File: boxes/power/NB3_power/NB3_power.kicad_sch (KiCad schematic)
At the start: 74 parts, among them J1 Barrel_Jack_PJ-036AH-SMT-TR, J2 Conn_01x02_Male, J3 Conn_01x02_Male, J4 Conn_01x02_Male, J5 Conn_01x04_Male, J6 Conn_01x02_Male, J7 Conn_01x02_Male, Q1 Q_PMOS_GDS, Q2 Q_NMOS_GDS, SW1 SW_SPDT, SW2 SW_SPDT, U1 NiMH_Charger_LTC4010, U2 Voltage_Regulator_AP64501

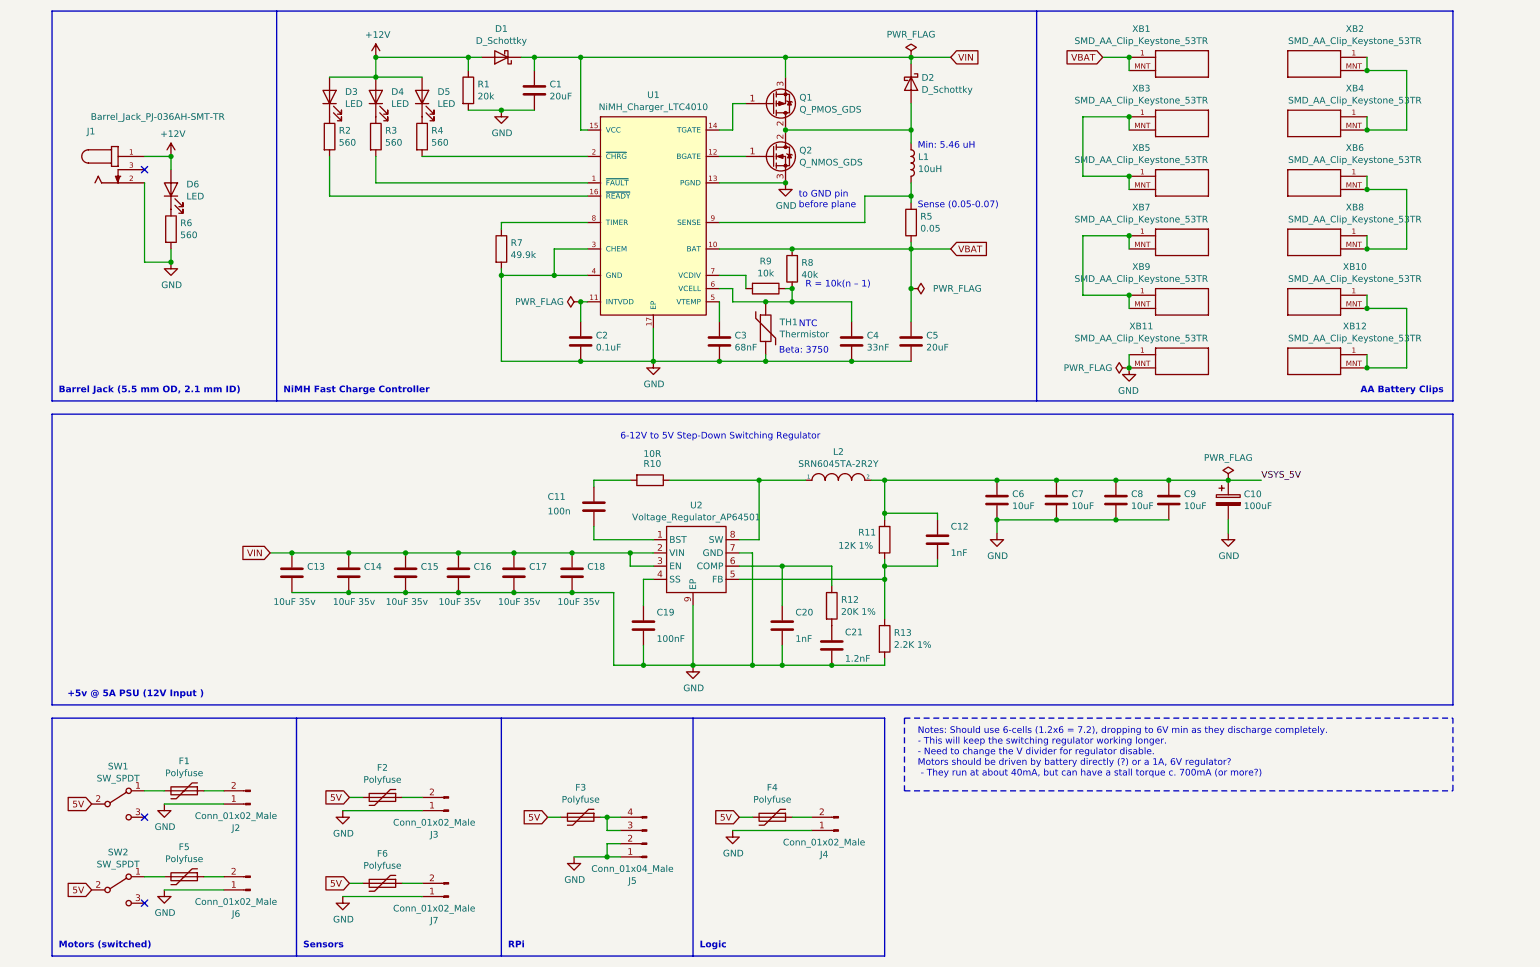
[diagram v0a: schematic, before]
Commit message: Work on NB3_power PCB
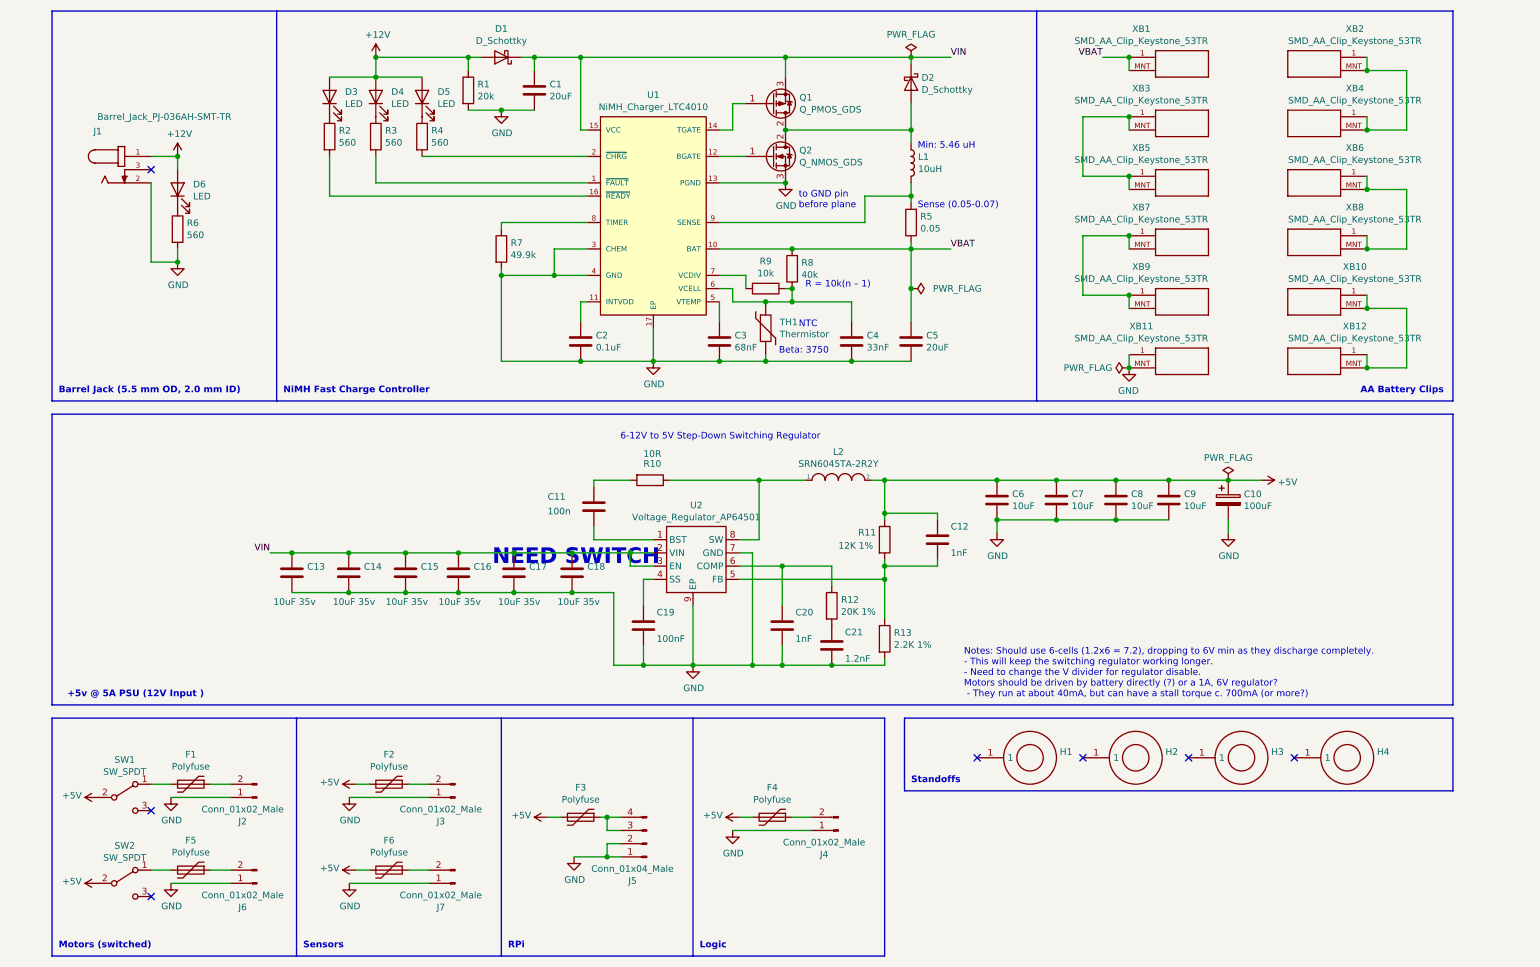
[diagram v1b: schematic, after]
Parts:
- added H1, H2, H3, H4: Standoff_SMT_5H_M2.5_9774050151R, NB3_power:Standoff_SMT_5H_M2.5_9774050151R, symbol NB3_power:Standoff_SMT_5H_M2.5_9774050151R
- Q1: footprint (none) -> NB3_power:PMOS_SMD_FDC658AP
- Q2: footprint (none) -> NB3_power:NMOS_SMD_SI3410DV-T1-GE3
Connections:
- net VSYS_5V is gone; now on net +5V: C10.1, C12.1, C6.1, C7.1, C8.1, C9.1, L2.2, R11.1
- net 5V renamed +5V
- no-connect marks 3 -> 7
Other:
- note added: "Barrel Jack (5.5 mm OD, 2.0 mm ID)"
- note added: "NEED SWITCH"
- note added: "Standoffs"
- note removed: "Barrel Jack (5.5 mm OD, 2.1 mm ID)"
- moved on the sheet: D6, F1, F2, F5, F6, J1, J2, J3, J6, J7, R6, SW1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

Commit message: More work on NB3_power PCB
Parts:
- removed D1, D2: D_Schottky, Diode_SMD:D_0805_2012Metric, symbol Device:D_Schottky
- removed SW2: SW_SPDT, NB3_power:Switch_SPDT_SMD_Slide_JS102011JCQN, symbol Switch:SW_SPDT
- added CR1, CR2: Schottky_PMEG3050EP,115, NB3_power:Schottky_PMEG3050EP,115, symbol NB3_power:Schottky_PMEG3050EP,115
- F1, F2, F4, F5, F6: value Polyfuse -> 1.1h2.2t
- F3: value Polyfuse -> 3h5t; footprint Fuse:Fuse_0805_2012Metric -> Fuse:Fuse_Bourns_MF-SM_7.98x5.44mm
- R8: value 40k -> 50k
- TH1: value Thermistor -> 10k, 3750; footprint (none) -> Resistor_SMD:R_0603_1608Metric
- renumbered C5 to C2, C2 to C3, C3 to C5, D3 to D1, D4 to D2, D5 to D3, D6 to D4, R6 to R5, R5 to R6
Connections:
- net +12V: now also CR1.2
- net +5V: now also F1.2, F5.2; no longer SW1.2 (B)
- net GND: now also SW1.3 (C)
- net VBAT: now also CR2.2
- net VIN: now also L1.1, Q1.2 (D), Q2.2 (D), SW1.1 (A), CR1.1, CR2.1; no longer U2.3 (EN)
- net at C5.1, U1.5 (VTEMP): now also C4.1, R8.1, R9.1, TH1.1, U1.6 (VCELL)
- new net: SW1.2 (B), U2.3 (EN)
- no-connect marks 7 -> 5
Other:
- note added: "Fuse: MF-LSMF300X-2"
- note added: "Fuse: MF-PSMF110X-2"
- note added: "Motors"
- note added: "NTCS0603E3103FMT"
- note removed: "Motors (switched)"
- note removed: "NEED SWITCH"
- note removed: "Notes: Should use 6-cells (1.2x6 = 7.2), dropping to 6V min as they discharge completely. - This will keep the switching regulator working longer. - Need to change the V divider for regulator disable. Motors should be driven by battery directly (?) or a 1A, 6V regulator? - They run at about 40mA, but can have a stall torque c. 700mA (or more?)"
- moved on the sheet: C1, C13, C14, C15, C16, C17, C18, C2, C3, C4, C5, D1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

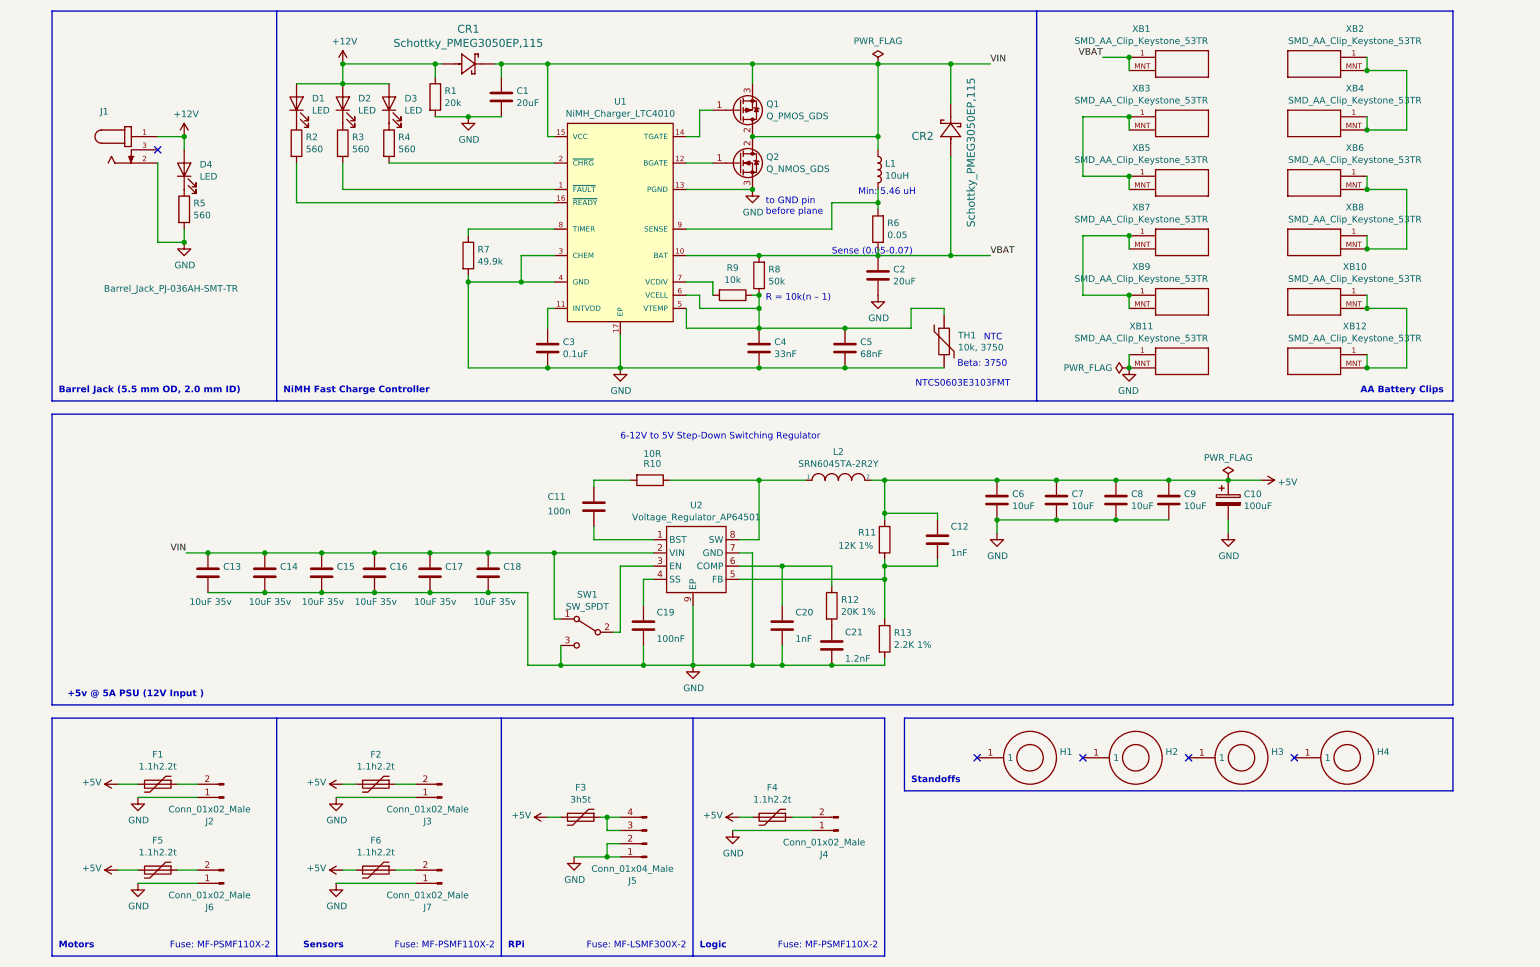
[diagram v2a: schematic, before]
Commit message: Work on NB3_power PCB (layout)
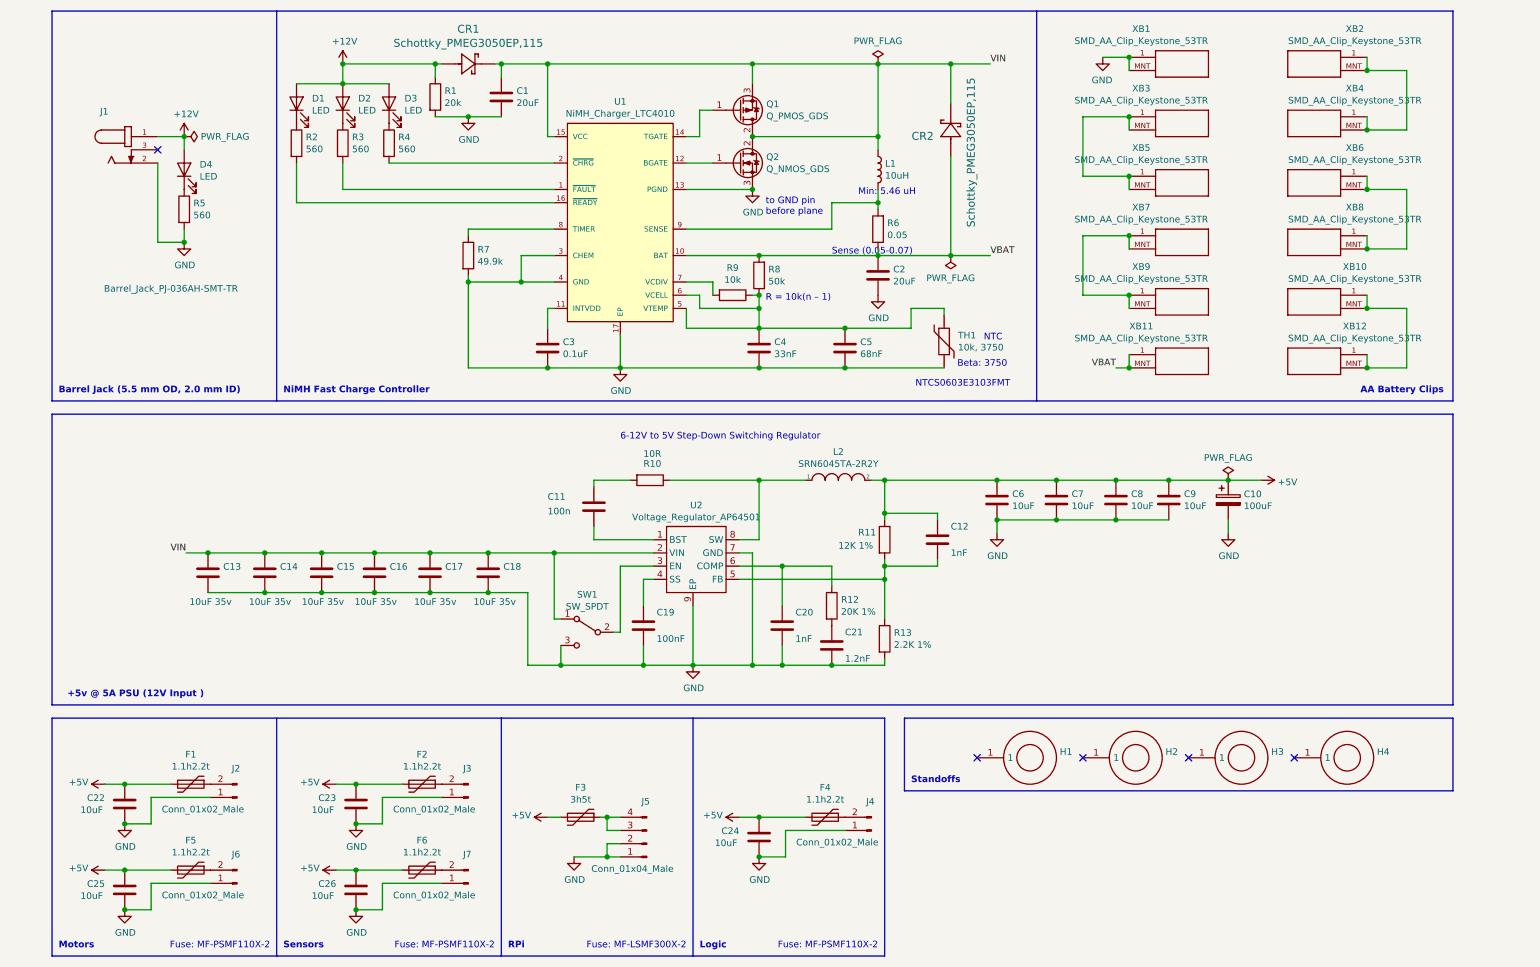
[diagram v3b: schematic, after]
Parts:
- added C22, C23, C24, C25, C26: 10uF, Capacitor_SMD:C_0805_2012Metric, symbol Device:C
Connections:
- net +5V: now also C22.1, C23.1, C24.1, C25.1, C26.1
- net GND: now also XB1.1, XB1.MNT, C22.2, C23.2, C24.2, C25.2, C26.2; no longer XB11.1, XB11.MNT
- net VBAT: now also XB11.1, XB11.MNT; no longer XB1.1, XB1.MNT
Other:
- moved on the sheet: F4, J2, J3, J4, J6, J7

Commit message: More work on NB£_power PCB
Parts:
- removed Q1: Q_PMOS_GDS, NB3_power:PMOS_SMD_FDC658AP, symbol Device:Q_PMOS_GDS
- removed Q2: Q_NMOS_GDS, NB3_power:NMOS_SMD_SI3410DV-T1-GE3, symbol Device:Q_NMOS_GDS
- added Q1: PMOS, NB3_power:PMOS_SMD_FDC658AP, symbol NB3_power:PMOS_SMD_FDC658AP
- added Q2: NMOS, NB3_power:NMOS_SMD_SI3410DV-T1-GE3, symbol NB3_power:NMOS_SMD_SI3410DV-T1-GE3
- J2, J3, J4, J6, J7: footprint Connector_PinHeader_2.54mm:PinHeader_1x02_P2.54mm_Vertical_SMD_Pin1Left -> Connector_PinHeader_2.54mm:PinHeader_1x02_P2.54mm_Vertical_SMD_Pin1Right
- J5: footprint Connector_PinHeader_2.54mm:PinHeader_1x04_P2.54mm_Vertical_SMD_Pin1Left -> Connector_PinHeader_2.54mm:PinHeader_1x04_P2.54mm_Vertical_SMD_Pin1Right
- L1: footprint Inductor_SMD:L_0805_2012Metric -> Inductor_SMD:L_Bourns_SRN6045TA
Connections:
- net GND: now also Q2.4 (S)
- net VIN: now also Q1.4 (S); no longer L1.1
- net at U1.12 (BGATE): now also Q2.3 (G)
- net at U1.14 (TGATE): now also Q1.3 (G)
- new net Drain: L1.1, Q1.1 (D), Q1.2 (D), Q1.5 (D), Q1.6 (D), Q2.1 (D), Q2.2 (D), Q2.5 (D), Q2.6 (D)

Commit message: Still NB3_power PCB
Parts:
- removed C10: 100uF, Capacitor_Tantalum_SMD:CP_EIA-7343-31_Kemet-D, symbol Device:CP
- added C10: 100uF, Capacitor_Tantalum_SMD:CP_EIA-7343-31_Kemet-D, symbol Device:C_Polarized
- C11: value 100n -> 100nF
- C3: value 0.1uF -> 100nF; footprint Capacitor_SMD:C_0603_1608Metric -> Capacitor_SMD:C_0402_1005Metric
- C4, C5: footprint Capacitor_SMD:C_0603_1608Metric -> Capacitor_SMD:C_0402_1005Metric
- L1: value 10uH -> SRN6045TA-6R3M
- R1, R2, R3, R4, R5, R7, R8, R9: footprint Resistor_SMD:R_0603_1608Metric -> Resistor_SMD:R_0402_1005Metric
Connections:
- net +5V: now also C10.1
- net GND: now also C10.2
